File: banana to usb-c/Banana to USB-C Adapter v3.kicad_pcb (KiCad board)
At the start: 2 copper layers, 34.3 x 26.6 mm, 32 parts, among them J1 USB4125-GF-A-0190, J2 Positive, J3 Negative

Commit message: sch: changed resistors to pull-up and added link to kb article
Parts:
- R3, R4: value 5k1 -> 56k
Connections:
- R3 pad 1: Net-(J1-CC1) -> /Positive
- R3 pad 2: GND -> Net-(J1-CC1)
- R4 pad 1: Net-(J1-CC2) -> /Positive
- R4 pad 2: GND -> Net-(J1-CC2)

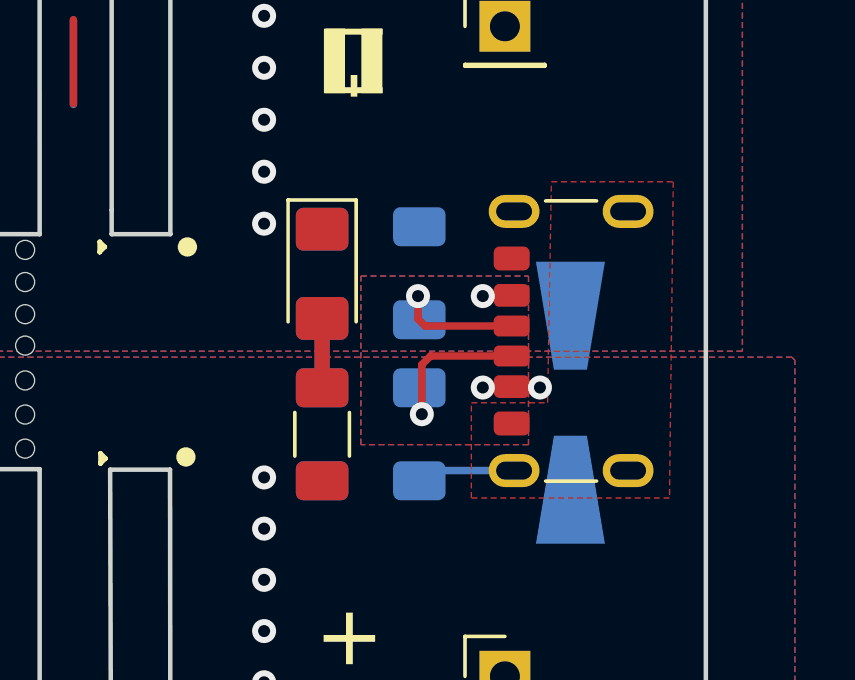
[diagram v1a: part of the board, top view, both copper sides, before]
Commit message: updated usbc pcb, generated v3 gerbs
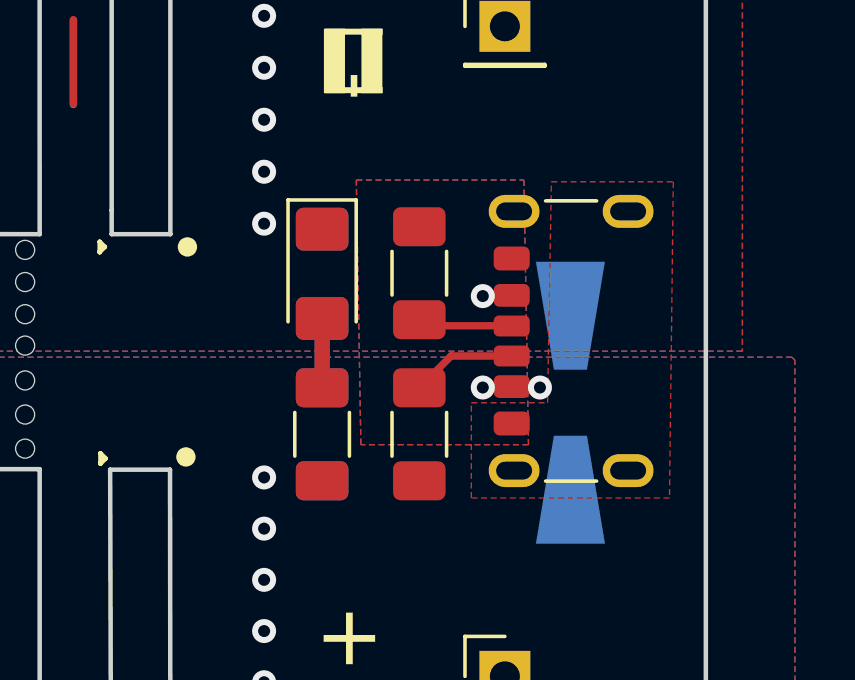
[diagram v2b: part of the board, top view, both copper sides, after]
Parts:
- R3, R4: moved to F.Cu
- turned R3 to 90 degrees
- turned R4 to -90 degrees
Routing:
- net GND: track 8.90 -> 5.60 mm
- net Net-(J1-CC1): track 5.68 -> 3.52 mm, vias 1 -> 0
- net Net-(J1-CC2): track 4.91 -> 3.50 mm, vias 1 -> 0
